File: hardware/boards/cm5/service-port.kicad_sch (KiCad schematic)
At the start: 5 parts, among them J501 USB4105-GF-A-120, SW501 SKRTLAE010, U501 TPD4E05U06DQAR

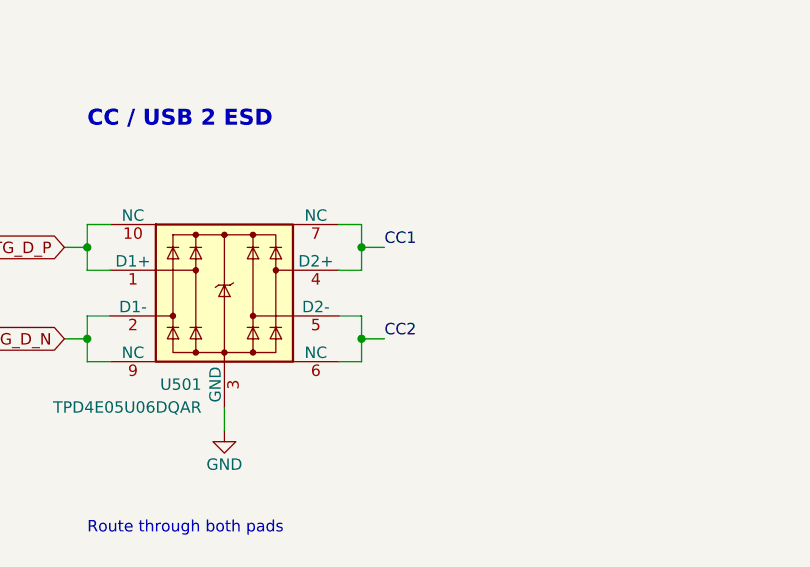
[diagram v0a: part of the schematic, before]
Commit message: feat(cm5): route the side board
Every net routed and DRC clean with schematic parity. Pairs are length matched; slow lines run as
45-degree diagonals, with In3 carrying the long cross-board runs (RPIBOOT, CM5_3V3, the PCIe
sideband, VBUS_EN) under the outer layers' high-speed walls.

The board is 102 mm deep like the main board, with five mounting holes at the corners and beside
the rear ports. The service port joins its D pins over and under the receptacle's pad row, and
U501's CC channels follow the connector's order so both CC lines run straight to R501 and R502.
The jack LED resistors sit west of the jack, R101 beside the fan header and R406 beside Q401.
The MDI pairs have no ESD array, as on the CM5 IO board. SW501's twin pin-1 pads are marked as
jumpered.
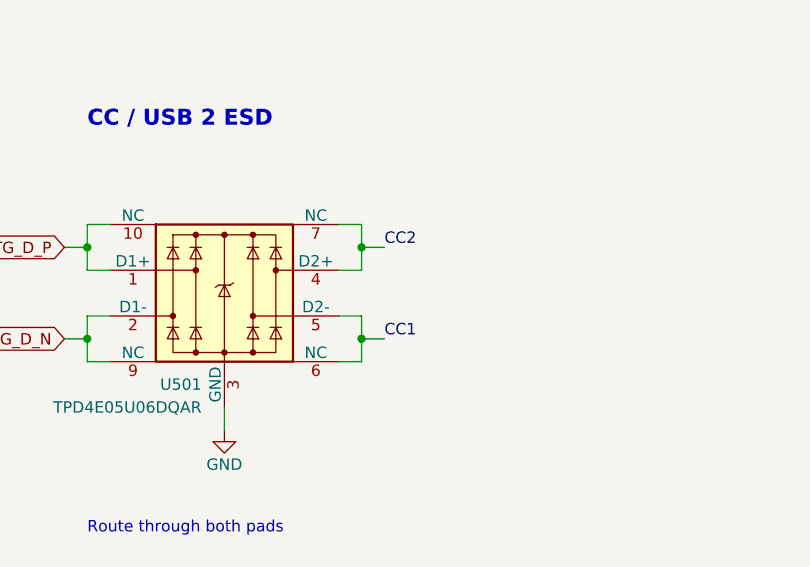
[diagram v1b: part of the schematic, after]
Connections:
- net CC1: now also U501.5 (D2-), U501.6 (NC); no longer U501.4 (D2+), U501.7 (NC)
- net CC2: now also U501.4 (D2+), U501.7 (NC); no longer U501.5 (D2-), U501.6 (NC)
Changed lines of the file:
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@@
 (global_label "OTG_D_P" (shape bidirectional) (at 134.62 134.62 180) (effects (font (size 1.27 1.27)) (justify right)) (property "Intersheetrefs" "${INTERSHEET_REFS}" (at 134.62 134.62 0) (hide yes) (effects (font (size 1.27 1.27)))))
 (global_label "OTG_D_N" (shape bidirectional) (at 134.62 144.78 180) (effects (font (size 1.27 1.27)) (justify right)) (property "Intersheetrefs" "${INTERSHEET_REFS}" (at 134.62 144.78 0) (hide yes) (effects (font (size 1.27 1.27)))))
-(label "CC1" (at 170.18 134.62 0) (effects (font (size 1.27 1.27)) (justify left bottom)))
-(label "CC2" (at 170.18 144.78 0) (effects (font (size 1.27 1.27)) (justify left bottom)))
+(label "CC2" (at 170.18 134.62 0) (effects (font (size 1.27 1.27)) (justify left bottom)))
+(label "CC1" (at 170.18 144.78 0) (effects (font (size 1.27 1.27)) (justify left bottom)))
 (no_connect (at 210.82 73.66))
 (no_connect (at 210.82 101.6))

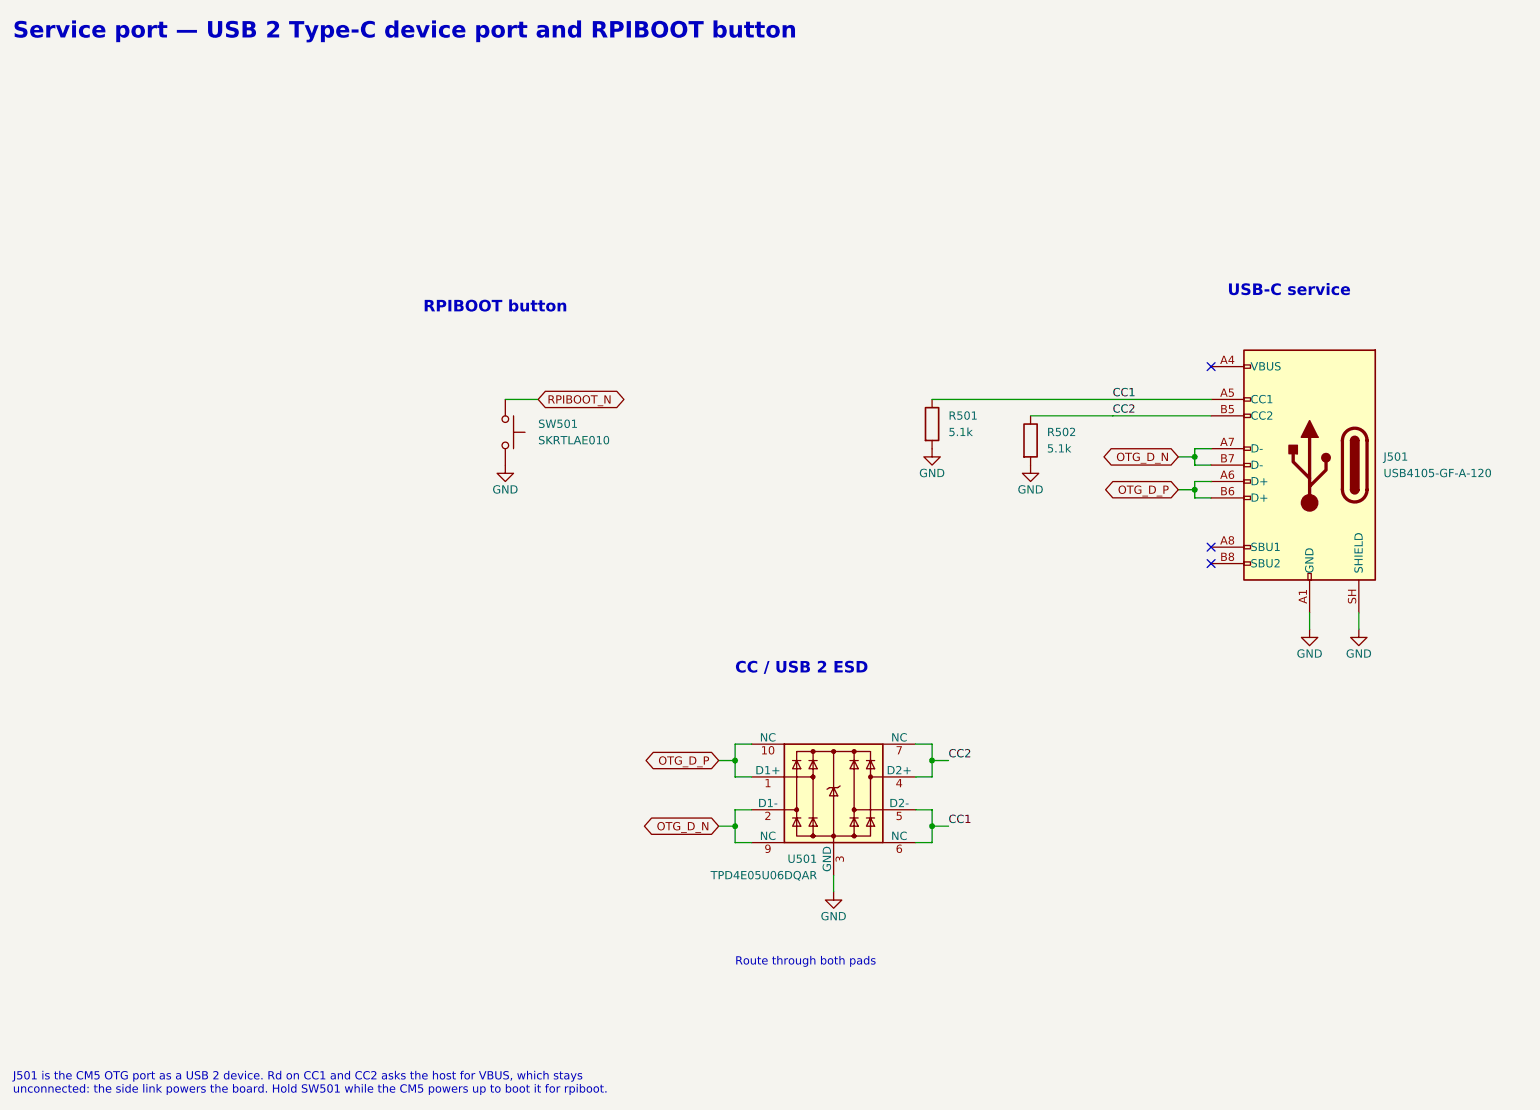
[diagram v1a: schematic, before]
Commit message: feat(hardware): use stocked CM5 headers
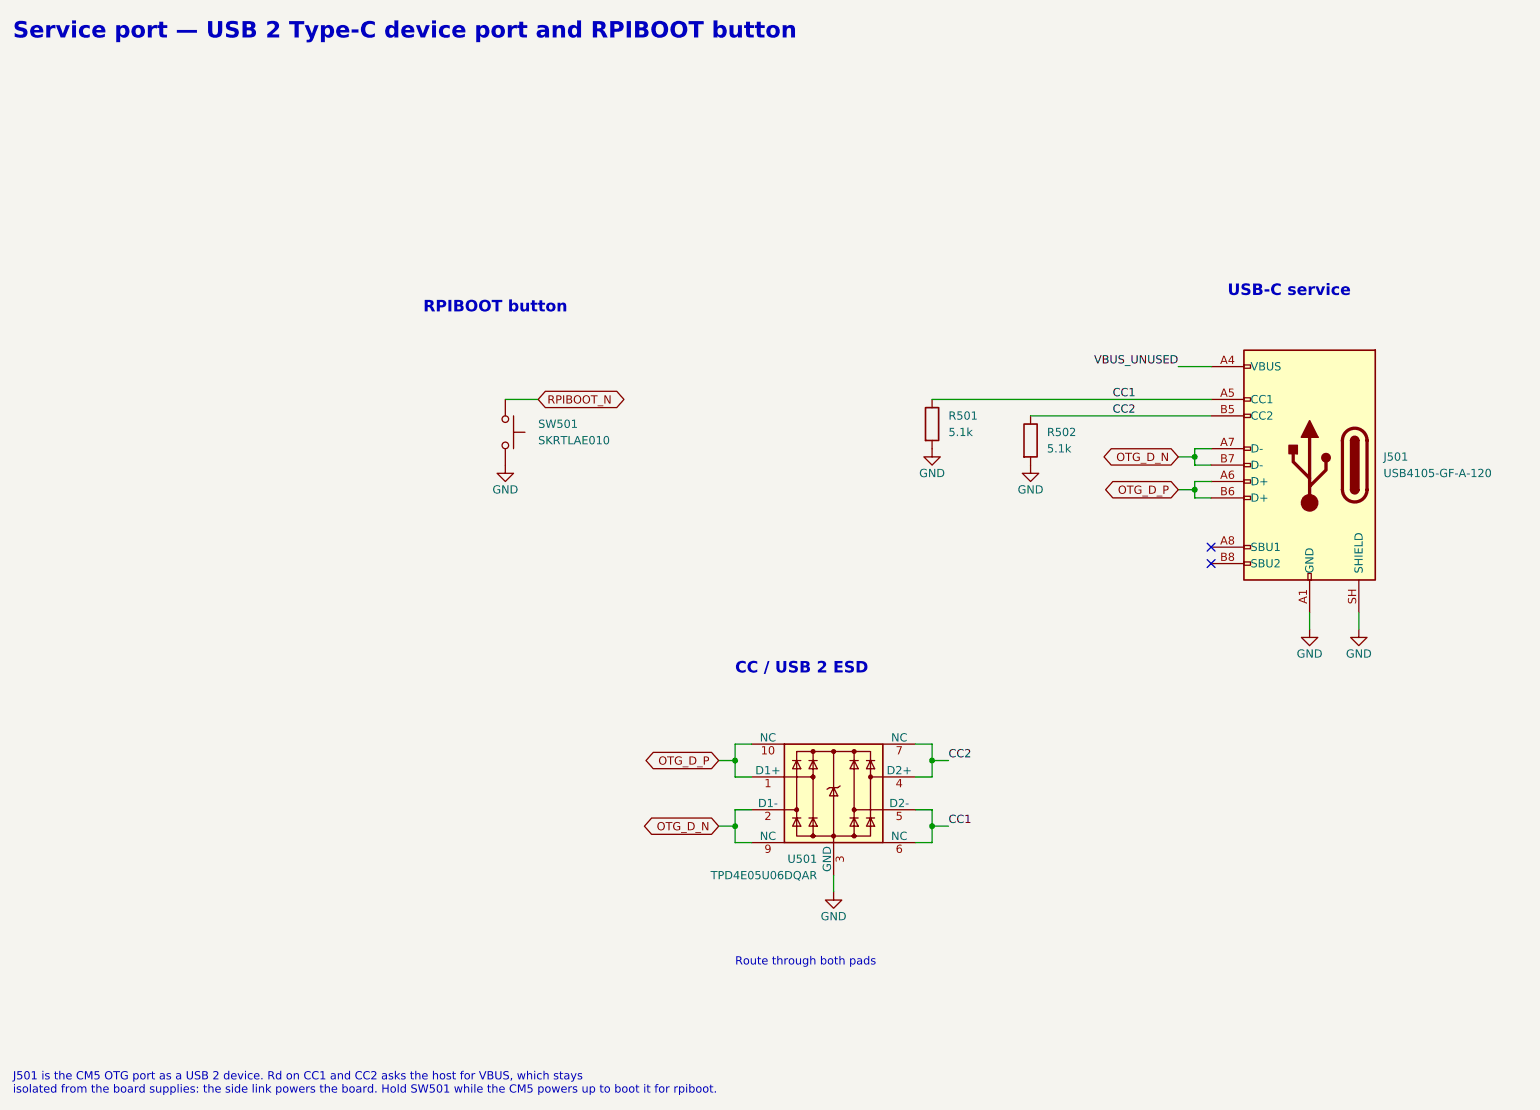
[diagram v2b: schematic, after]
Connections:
- net VBUS_UNUSED: now reaches J501.A4 (VBUS), J501.A9 (VBUS), J501.B4 (VBUS), J501.B9 (VBUS)
- no-connect marks 3 -> 2
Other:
- note added: "J501 is the CM5 OTG port as a USB 2 device. Rd on CC1 and CC2 asks the host for VBUS, which stays isolated from the board supplies: the side link powers the board. Hold SW501 while the CM5 powers up to boot it for rpiboot."
- note removed: "J501 is the CM5 OTG port as a USB 2 device. Rd on CC1 and CC2 asks the host for VBUS, which stays unconnected: the side link powers the board. Hold SW501 while the CM5 powers up to boot it for rpiboot."
